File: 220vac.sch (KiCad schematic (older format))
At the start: 4 parts, among them J1 220VAC in, T1 Transformer

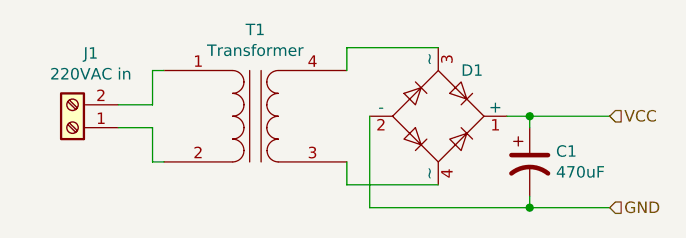
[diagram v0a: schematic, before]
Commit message: Fixed ERC errors, combined all outputs into a bus, fixed annotations
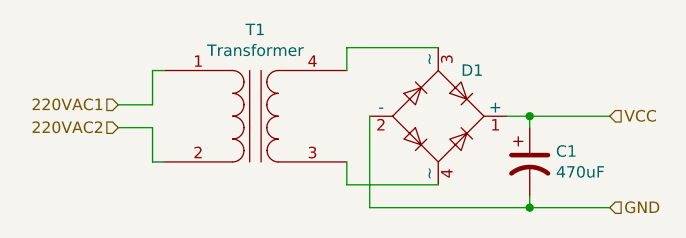
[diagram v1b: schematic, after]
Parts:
- removed J1: 220VAC in, symbol Connector:Screw_Terminal_01x02
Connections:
- net 220VAC2: now reaches T1.2 (AB)
- net 220VAC1: now reaches T1.1 (AA)
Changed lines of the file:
@@
 Text HLabel 4300 2650 2    50   Input ~ 0
 GND
-$Comp
-L Connector:Screw_Terminal_01x02 J1
-U 1 1 5E68943B
-P 1950 2300
-F 0 "J1" H 1870 1975 50  0000 C CNN
-F 1 "220VAC in" H 1870 2066 50  0000 C CNN
-F 2 "" H 1950 2300 50  0001 C CNN
-F 3 "~" H 1950 2300 50  0001 C CNN
-	1    1950 2300
-	-1   0    0    1
-$EndComp
+Text HLabel 2150 2200 0    50   Input ~ 0
+220VAC1
+Text HLabel 2150 2300 0    50   Input ~ 0
+220VAC2
 $EndSCHEMATC

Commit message: Added AC->DC transformer ratio
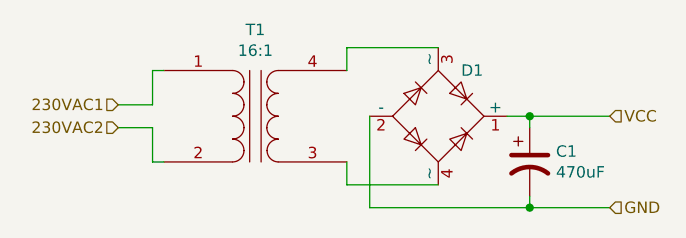
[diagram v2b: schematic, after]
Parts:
- T1: value Transformer -> 16:1
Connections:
- net 220VAC1 renamed 230VAC1
- net 220VAC2 renamed 230VAC2
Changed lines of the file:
@@
 P 2750 2250
 F 0 "T1" H 2750 2628 50  0000 C CNN
-F 1 "Transformer" H 2750 2537 50  0000 C CNN
+F 1 "16:1" H 2750 2537 50  0000 C CNN
 F 2 "" H 2750 2250 50  0001 C CNN
 F 3 "~" H 2750 2250 50  0001 C CNN
@@
 GND
 Text HLabel 2150 2200 0    50   Input ~ 0
-220VAC1
+230VAC1
 Text HLabel 2150 2300 0    50   Input ~ 0
-220VAC2
+230VAC2
 $EndSCHEMATC
